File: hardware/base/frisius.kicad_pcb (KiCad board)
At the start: 4 copper layers, 50 x 50 mm, 96 parts, among them J1 MEM2067, J2 USB_C_Receptacle_USB2.0, J3 BATTERY, J4 Display, Q1 Q_Dual_NMOS_G1S2G2D2S1D1, SW1 RESET, SW2 BOOT, SW3 POWER, SW4 NAV, U2 FXOS8700CQR1, U3 MS5637-02BA03, U4 L96-M33, U6 ESP32-S3-WROOM-1, U7 TLV62569DBV, U8 MP2723, U9 MAX17048G

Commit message: schematic complete unreviewed
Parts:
- removed D10, D9: PESD3V3L2UM, Package_TO_SOT_SMD:SOT-883
- removed R59: 0, Resistor_SMD:R_0402_1005Metric
- added C2: 4.7u, Capacitor_SMD:C_0603_1608Metric, F.Cu at (-25.0, 236.4)
- added C26: 1u, Capacitor_SMD:C_0603_1608Metric, F.Cu at (-45.2, 217.1)
- added C27: 1u, Capacitor_SMD:C_0603_1608Metric, F.Cu at (-56.6, 225.8)
- added C28: 0.1u, Capacitor_SMD:C_0402_1005Metric, F.Cu at (-42.8, 223.3)
- added C29: 4.7u, Capacitor_SMD:C_0603_1608Metric, F.Cu at (-41.1, 235.9)
- added C30: 1u, Capacitor_SMD:C_0603_1608Metric, F.Cu at (-40.6, 231.9)
- added C31: 10p, Capacitor_SMD:C_0402_1005Metric, F.Cu at (-37.7, 237.6)
- added C32: 10u, Capacitor_SMD:C_0603_1608Metric, F.Cu at (-50.3, 236.3)
- added C33: 10u, Capacitor_SMD:C_0603_1608Metric, F.Cu at (-45.1, 235.9)
- added C34: 10u, Capacitor_SMD:C_0603_1608Metric, F.Cu at (-24.1, 175.6)
- added C37: 10u, Capacitor_SMD:C_0603_1608Metric, F.Cu at (-23.1, 173.9)
- added C38: 4.7u, Capacitor_SMD:C_0603_1608Metric, F.Cu at (-19.1, 173.9)
- added C39: 0.1u, Capacitor_SMD:C_0402_1005Metric, F.Cu at (-20.6, 175.3)
- added C40: 4.7u, Capacitor_SMD:C_0603_1608Metric, F.Cu at (-11.3, 205.5)
- added C41: 4.7u, Capacitor_SMD:C_0603_1608Metric, F.Cu at (40.8, 115.7)
- added J5: Conn_01x45_Shielded, Connector_FFC-FPC:Hirose_FH12-45S-0.5SH_1x45-1MP_P0.50mm_Horizontal, F.Cu at (99.6, 105.4)
- added J6: CapTouch, Connector_FFC-FPC:TE_0-1734839-8_1x08-1MP_P0.5mm_Horizontal, F.Cu at (115.3, 88.7)
- added J7: I2C ISENSE, Connector_PinHeader_2.54mm:PinHeader_1x04_P2.54mm_Vertical, F.Cu at (66.3, 106.8)
- added L3: 1u, Inductor_SMD:L_Wuerth_MAPI-2510, F.Cu at (-44.9, 232.6)
- added Q2: Q_NMOS_DGS, Package_TO_SOT_SMD:SOT-323_SC-70, F.Cu at (-58.9, 166.6)
- added Q3: Q_NMOS_DGS, Package_TO_SOT_SMD:SOT-323_SC-70, F.Cu at (-54.5, 166.6)
- added R13: 100k, Resistor_SMD:R_0402_1005Metric, F.Cu at (-42.8, 220.3)
- added R14: 100k, Resistor_SMD:R_0402_1005Metric, F.Cu at (-34.1, 216.8)
- added R15: 100k, Resistor_SMD:R_0402_1005Metric, F.Cu at (-37.0, 216.8)
- added R16: 4.7k, Resistor_SMD:R_0402_1005Metric, F.Cu at (-45.7, 221.3)
- added R17: 4.7k, Resistor_SMD:R_0402_1005Metric, F.Cu at (-37.0, 218.8)
- added R18: 4.7k, Resistor_SMD:R_0402_1005Metric, F.Cu at (-37.0, 220.8)
- added R42: R_Shunt, bt_Resistor:R_0805_4WKelvin, F.Cu at (38.0, 116.2)
- added R43: 100k, Resistor_SMD:R_0402_1005Metric, F.Cu at (-34.8, 235.6)
- added R44: 0, Resistor_SMD:R_0402_1005Metric, F.Cu at (-37.7, 235.6)
- added R45: R_Shunt, bt_Resistor:R_0805_4WKelvin, F.Cu at (60.4, 99.0)
- added R46: 0, Resistor_SMD:R_0402_1005Metric, F.Cu at (-37.1, 233.6)
- added R47: 0, Resistor_SMD:R_0402_1005Metric, F.Cu at (-37.1, 231.6)
- added R48: 0, Resistor_SMD:R_0402_1005Metric, F.Cu at (-34.2, 233.6)
- added R49: 0, Resistor_SMD:R_0402_1005Metric, F.Cu at (-34.2, 231.6)
- added R50: R_Shunt, bt_Resistor:R_0805_4WKelvin, F.Cu at (54.9, 121.9)
- added R51: R_Shunt, bt_Resistor:R_0805_4WKelvin, F.Cu at (56.9, 101.3)
- added R52: 0, Resistor_SMD:R_0402_1005Metric, F.Cu at (-6.25, 202.0)
- added R53: 0, Resistor_SMD:R_0402_1005Metric, F.Cu at (-7.89, 205.2)
- added R54: 0, Resistor_SMD:R_0402_1005Metric, F.Cu at (-4.98, 204.0)
- added RN1: 100k, Resistor_SMD:R_Array_Concave_4x0402, F.Cu at (107.9, 109.8)
- added RN2: 100k, Resistor_SMD:R_Array_Concave_4x0402, F.Cu at (103.9, 109.8)
- added RN3: 100k, Resistor_SMD:R_Array_Concave_4x0402, F.Cu at (100.4, 109.8)
- added RN4: 100k, Resistor_SMD:R_Array_Concave_4x0402, F.Cu at (96.9, 109.8)
- added TP12: GPS_RST, TestPoint:TestPoint_Pad_D1.0mm, F.Cu at (-37.8, 166.3)
- added TP13: GPS_INT, TestPoint:TestPoint_Pad_D1.0mm, F.Cu at (-39.2, 170.0)
- added TP14: GPS_FON, TestPoint:TestPoint_Pad_D1.0mm, F.Cu at (-42.2, 170.0)
- added U1: PI4IOE5V9554A, Package_SO:TSSOP-16_4.4x5mm_P0.65mm, F.Cu at (71.7, 89.2)
- added U10: LTR-329ALS-01, Package_LGA:VLGA-4_2x2.5mm_P1.65mm, F.Cu at (-30.0, 177.0)
- added U11: AP2502, Package_TO_SOT_SMD:SOT-23-6, B.Cu at (-16.0, 210.6)
- added U12: PAC1944, Package_DFN_QFN:UQFN-16-1EP_4x4mm_P0.65mm_EP2.7x2.7mm, F.Cu at (61.1, 103.1)
- added U13: TLV62569DBV/AP3428, Package_TO_SOT_SMD:SOT-23-5, F.Cu at (-49.7, 232.8)
- added U14: EClamp2410P, bt_Package_DFN:UDFN-16-4x1.6_P0.5mm_EP3x0.5mm, F.Cu at (44.1, 73.5)
- added U5: FXOS8700CQR1, Package_LGA:LGA-16_3x3mm_P0.5mm_LayoutBorder3x5y, F.Cu at (-24.7, 232.9)
- C11, C9: value 4.7u -> 0.1u; footprint Capacitor_SMD:C_0603_1608Metric -> Capacitor_SMD:C_0402_1005Metric
- C21, C22: value 10u -> 4.7u
- C4: value 4.7u -> 1u
- D1, D3, D5: footprint LED_SMD:LED_0402_1005Metric -> LED_SMD:LED_0603_1608Metric
- D2: footprint LED_SMD:LED_0603_1608Metric -> Diode_SMD:D_SOD-123
- D4: footprint Package_TO_SOT_SMD:SOT-883 -> Package_TO_SOT_SMD:SOT-23
- D6: footprint LED_SMD:LED_0402_1005Metric -> LED_SMD:LED_0603_1608Metric; moved to F.Cu
- D7, D8: value PESD3V3L2UM -> LED_Small_Filled; footprint Package_TO_SOT_SMD:SOT-883 -> LED_SMD:LED_0603_1608Metric
- H1, H2, H3, H4, SW2, SW3, SW4: moved to F.Cu
- J4: value Display -> Debug UART; footprint Connector_Molex:Molex_SlimStack_55560-0241_2x12_P0.50mm_Vertical -> Connector_PinHeader_2.54mm:PinHeader_1x03_P2.54mm_Vertical; moved to F.Cu
- Q1: value Q_Dual_NMOS_G1S2G2D2S1D1 -> Q_NMOS_DGS; footprint Package_TO_SOT_SMD:SOT-363_SC-70-6 -> Package_TO_SOT_SMD:SOT-323_SC-70
- R1, R6: value R_Small -> 100k
- R10, R11, R12, R8: value 10k -> 100k
- R2, R7: value 10k -> 1k
- R34: value 0 -> 14k
- R35: value 14k -> ?
- R40: value R_Small -> 4.7k
- U2: value FXOS8700CQR1 -> 74CBTLV3257; footprint Package_LGA:LGA-16_3x3mm_P0.5mm_LayoutBorder3x5y -> Package_SO:TSSOP-16_4.4x5mm_P0.65mm
- U3: value MS5637-02BA03 -> ESP32-S3-WROOM-1-PinOrder; footprint bt_Package_LGA:TE_MS563702BA03-50 -> bt_Espressif:ESP32-S3-WROOM-1U
- U6: value ESP32-S3-WROOM-1 -> MS5637-02BA03; footprint bt_Espressif:ESP32-S3-WROOM-1U -> bt_Package_LGA:TE_MS563702BA03-50
- U7: value TLV62569DBV -> TLV62569DBV/AP3428
- moved R40 171.1 mm to (-53.2, 225.5), turned to 0 degrees
- moved SW2 158.6 mm to (-38.6, 226.6), turned to 0 degrees
- moved R10 157.7 mm to (-45.7, 219.3), turned to 0 degrees
- moved C14 157.0 mm to (-21.0, 233.6), turned to 0 degrees
- moved R8 156.7 mm to (-31.4, 228.9), turned to 0 degrees
- moved C13 156.3 mm to (-18.7, 235.5)
- moved C15 152.1 mm to (-21.6, 236.1), turned to 0 degrees
- moved C16 152.1 mm to (-15.2, 231.6)
- moved C12 151.7 mm to (-18.1, 233.6), turned to 0 degrees
- moved R12 151.6 mm to (-39.9, 220.3), turned to 0 degrees
- moved R9 150.5 mm to (-21.0, 231.6), turned to 0 degrees
- moved C11 149.8 mm to (-18.1, 231.6), turned to 0 degrees
- moved R11 147.3 mm to (-34.1, 218.8), turned to 0 degrees
- moved C3 143.2 mm to (-26.5, 219.8)
- moved SW1 142.1 mm to (-26.1, 202.5)
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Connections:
- C1 pad 1: +3V3 -> VDD_CORE_3V3
- C11 pad 1: +3V3 -> VDD_AUX_3V3
- C12 pad 1: +3V3 -> VDD_AUX_3V3
- C13 pad 1: +3V3 -> Net-(C13-Pad1)
- C14 pad 1: Net-(C14-Pad1) -> VDD_AUX_3V3
- C15 pad 1: +3V3 -> VDD_AUX_3V3
- C17 pad 1: VDD_NVDC -> VDD_AUX_3V3
- C18 pad 1: +3V3 -> VDD_AUX_3V3
- C19 pad 1: +3V3 -> VDD_AUX_3V3
- C21 pad 1: /Power/VREF -> VBUS
- C22 pad 1: +BATT -> VBUS
- C3 pad 1: +3V3 -> VDD_AUX_3V3
- C35 pad 1: VBUS -> Net-(C35-Pad1)
- C36 pad 1: VBUS -> Net-(C35-Pad1)
- C6 pad 1: +3V3 -> Net-(C6-Pad1)
- C7 pad 1: +3V3 -> VDD_CORE_3V3
- C8 pad 1: +3V3 -> VDD_CORE_3V3
- C9 pad 1: VBUS -> VDD_AUX_3V3
- D2 pad 1: Net-(D2-Pad1) -> /Power/CORE_ENABLE
- D2 pad 2: Net-(D2-Pad2) -> /Power/BOOTSTRAP
- D5 pad 1: GND -> Net-(D5-Pad1)
- D7 pad 1: /Processor/SDMMC.D0 -> GND
- D7 pad 2: /Processor/SDMMC.D1 -> Net-(D7-Pad2)
- D8 pad 1: /Processor/SDMMC.CMD -> GND
- D8 pad 2: /Processor/SDMMC.CLK -> Net-(D8-Pad2)
- J1 pad 1: /Processor/SDMMC.D2 -> Net-(J1-Pad1)
- J1 pad 2: /Processor/SDMMC.D3 -> Net-(J1-Pad2)
- J1 pad 3: /Processor/SDMMC.CMD -> Net-(J1-Pad3)
- J1 pad 4: +3V3 -> VDD_AUX_3V3
- J1 pad 5: /Processor/SDMMC.CLK -> Net-(J1-Pad5)
- J1 pad 7: /Processor/SDMMC.D0 -> Net-(J1-Pad7)
- J1 pad 8: /Processor/SDMMC.D1 -> Net-(J1-Pad8)
- J2 pad A4: VBUS -> Net-(C35-Pad1)
- J2 pad A9: VBUS -> Net-(C35-Pad1)
- J2 pad B4: VBUS -> Net-(C35-Pad1)
- J2 pad B9: VBUS -> Net-(C35-Pad1)
- J4 pad 2: GND -> /Processor/DEBUG_RX
- J4 pad 3: +3V3 -> /Processor/DEBUG_TX
- L1 pad 2: +3V3 -> Net-(C6-Pad1)
- Q1 pad 1: Net-(D2-Pad2) -> Net-(D5-Pad1)
- Q1 pad 2: GND -> /GPS/GPS_FIX
- Q1 pad 3: /Power/SHUTDOWN -> GND
- R1 pad 1: +3V3 -> VDD_CORE_3V3
- R1 pad 2: /Processor/RST_BTN -> ~{RESET}
- R10 pad 1: +3V3 -> VDD_AUX_3V3
- R10 pad 2: /Processor/SDMMC.CMD -> /Display/IM2
- R11 pad 1: +3V3 -> /Display/IM2
- R11 pad 2: /Processor/SDMMC.D3 -> GND
- R12 pad 1: +3V3 -> VDD_AUX_3V3
- R12 pad 2: /Processor/SDMMC.D2 -> /Display/IM1
- R2 pad 1: Net-(R2-Pad1) -> Net-(D7-Pad2)
- R2 pad 2: GND -> /Processor/STATUS_IOEXP0
- R23 pad 2: +3V3 -> VDD_CORE_3V3
- R24 pad 1: /Power/PORT_D- -> /Power/PORT_D+
- R24 pad 2: /Power/USB_CHG.D- -> /Power/USB_CHG.D+
- R25 pad 1: /Power/PORT_D+ -> /Power/PORT_D-
- R25 pad 2: /Power/USB_CHG.D+ -> /Power/USB_CHG.D-
- R27 pad 1: Net-(D2-Pad1) -> /Power/CORE_ENABLE
- R27 pad 2: +3V3 -> VDD_CORE_3V3
- R28 pad 2: /GPS/L96_FIX -> VDD_AUX_3V3
- R29 pad 1: +3V3 -> Net-(C6-Pad1)
- R3 pad 1: +3V3 -> VDD_AUX_3V3
- R31 pad 1: /Power/VREF -> Net-(C37-Pad1)
- R32 pad 1: /Power/VREF -> Net-(C37-Pad1)
- R33 pad 1: Net-(R33-Pad1) -> /Power/PORT_D+
- R33 pad 2: GND -> /Power/USB_ESP.D+
- R35 pad 1: Net-(R35-Pad1) -> Net-(C31-Pad1)
- R35 pad 2: GND -> Net-(C31-Pad2)
- R37 pad 2: Net-(R36-Pad2) -> Net-(R36-Pad1)
- R4 pad 1: +3V3 -> VDD_AUX_3V3
- R40 pad 1: +3V3 -> /Display/SYS_I2C.SCL
- R40 pad 2: /Processor/NAV_BTN -> VDD_AUX_3V3
- R41 pad 2: Net-(R41-Pad2) -> /Processor/STATUS_ESP
- R6 pad 1: +3V3 -> VDD_CORE_3V3
- R7 pad 1: +3V3 -> Net-(D8-Pad2)
- R7 pad 2: /Processor/SDMMC.D1 -> /Processor/STATUS_IOEXP1
- R8 pad 1: +3V3 -> VDD_CORE_3V3
- R8 pad 2: /Processor/SDMMC.D0 -> /Processor/NAV_BTN
- R9 pad 1: +3V3 -> Net-(R9-Pad1)
- R9 pad 2: /Processor/SDMMC.CLK -> GND
- SW1 pad 2: /Processor/RST_BTN -> ~{RESET}
- SW3 pad 2: Net-(D2-Pad2) -> /Power/BOOTSTRAP
- U2 pad 1: +3V3 -> /Display/LCD_SPI_CS
- U2 pad 10: GND -> /Display/LCD_CTRL.HSYNC
- U2 pad 11: unconnected-(U2-Pad11) -> /Display/LCD_SPI.MOSI
- U2 pad 12: GND -> /Display/LCD_MUX3
- U2 pad 13: GND -> /Display/LCD_CTRL.VSYNC
- U2 pad 14: +3V3 -> /Display/LCD_SPI.MISO
- U2 pad 15: unconnected-(U2-Pad15) -> GND
- U2 pad 16: Net-(R2-Pad1) -> VDD_AUX_3V3
- U2 pad 2: Net-(C14-Pad1) -> /Display/LCD_SPI.DC
- U2 pad 3: GND -> /Display/LCD_CTRL.DE
- U2 pad 4: /Display/SYS_I2C.SCL -> /Display/LCD_MUX0
- U2 pad 5: GND -> /Display/LCD_SPI.SCLK
- U2 pad 6: /Display/SYS_I2C.SDA -> /Display/LCD_CTRL.PCLK
- U2 pad 7: GND -> /Display/LCD_MUX1
- U2 pad 8: Net-(C16-Pad1) -> GND
- U2 pad 9: unconnected-(U2-Pad9) -> /Display/LCD_MUX2
- U3 pad 1: +3V3 -> GND
- U3 pad 2: /Display/SYS_I2C.SDA -> VDD_CORE_3V3
- U3 pad 3: /Display/SYS_I2C.SCL -> ~{RESET}
- U3 pad 4: GND -> /Processor/SDMMC.D3
- U4 pad 2: /GPS/L96_FIX -> /GPS/GPS_FIX
- U4 pad 23: Net-(TP12-Pad1) -> ~{RESET}
- U4 pad 28: Net-(TP14-Pad1) -> /GPS/GPS_FORCE_ON
- U4 pad 8: VDD_NVDC -> VDD_AUX_3V3
- U4 pad 9: +3V3 -> VDD_AUX_3V3
- U6 pad 1: GND -> VDD_AUX_3V3
- U6 pad 2: +3V3 -> /Display/SYS_I2C.SDA
- U6 pad 3: /Processor/RST_BTN -> /Display/SYS_I2C.SCL
- U6 pad 4: unconnected-(U6-Pad4) -> GND
- U7 pad 1: Net-(D2-Pad1) -> /Power/CORE_ENABLE
- U8 pad 11: Net-(R36-Pad2) -> Net-(R36-Pad1)
- U8 pad 12: Net-(R36-Pad1) -> Net-(R36-Pad2)
- U8 pad 13-14: /Power/VREF -> Net-(C37-Pad1)
- U8 pad 17: +BATT -> Net-(R50-Pad1)
- U8 pad 18: Net-(R34-Pad1) -> Net-(R46-Pad1)
- U8 pad 23: Net-(R33-Pad1) -> Net-(R44-Pad1)
- U8 pad 24: Net-(R35-Pad1) -> Net-(R34-Pad1)
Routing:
- net /Display/SYS_I2C.SDA: track 24.3 -> 0.00 mm, vias 4 -> 0
- added copper zone on F.Cu, net VDD_AUX_3V3
- removed copper zone on F.Cu, net +3V3
- removed copper zone on In2.Cu, net +3V3
- removed copper zone on B.Cu, net GND
- removed copper zone on F.Cu, net GND
- removed copper zone on In1.Cu, net GND
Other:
- board size 50 x 50 mm -> 100 x 85 mm
- board text added: "3V GND RST TI TD TC SO SI SC DC CS"
- board text added: "BL R0 R1 G0 G1 B0 B1 DE PC HS VS"

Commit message: placed components on board - rough
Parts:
- removed C40: 4.7u, Capacitor_SMD:C_0603_1608Metric
- TP12, TP13, TP14: moved to B.Cu
- U11: moved to F.Cu
- moved SW2 220.1 mm to (108.6, 63.0), turned to 180 degrees
- moved R40 218.7 mm to (114.7, 85.3), turned to 90 degrees
- moved R16 212.5 mm to (117.7, 85.3), turned to 90 degrees
- moved C28 207.2 mm to (113.3, 87.1), turned to 180 degrees
- moved R18 204.0 mm to (115.7, 85.3), turned to 90 degrees
- moved SW3 203.6 mm to (98.6, 63.0), turned to 180 degrees
- moved R17 203.5 mm to (116.7, 85.3), turned to 90 degrees
- moved R8 203.0 mm to (88.6, 65.2)
- moved SW4 202.9 mm to (88.6, 63.0)
- moved R6 198.5 mm to (108.6, 65.2), turned to 180 degrees
- moved R13 189.3 mm to (111.9, 111.3), turned to 90 degrees
- moved R10 189.1 mm to (110.9, 113.3), turned to 90 degrees
- moved R12 185.7 mm to (111.9, 113.3), turned to 90 degrees
- moved C27 185.7 mm to (89.3, 110.9), turned to 180 degrees
- moved R15 183.3 mm to (112.9, 111.3), turned to 90 degrees
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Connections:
- C17 pad 1: VDD_AUX_3V3 -> VDD_NVDC
- U12 pad 10: /Power/VAUX_S+ -> /Power/VCORE_S+
- U12 pad 7: /Power/VCORE_S- -> /Power/VAUX_S-
- U12 pad 8: /Power/VCORE_S+ -> /Power/VAUX_S+
- U12 pad 9: /Power/VAUX_S- -> /Power/VCORE_S-
- U3 pad 15: /Display/LCD_RGB.R2 -> /Display/LCD_RGB.R0
- U3 pad 17: /Display/LCD_RGB.R0 -> /Display/LCD_RGB.R2
- U3 pad 18: /Display/LCD_RGB.G2 -> /Display/LCD_RGB.G0
- U3 pad 20: /Display/LCD_RGB.G0 -> /Display/LCD_RGB.G2
- U3 pad 21: /Display/LCD_RGB.B1 -> /Display/LCD_RGB.B0
- U3 pad 22: /Display/LCD_RGB.B0 -> /Display/LCD_RGB.B1
- U4 pad 8: VDD_AUX_3V3 -> VDD_NVDC
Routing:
- net VDD_NVDC: track 0.00 -> 11.9 mm
- net Net-(C10-Pad2): track 0.00 -> 9.25 mm
- net Net-(R50-Pad1): track 0.00 -> 5.85 mm
- net VBUS: track 0.00 -> 4.59 mm
- net Net-(C23-Pad1): track 0.00 -> 2.47 mm
- net Net-(C37-Pad1): track 0.00 -> 2.35 mm
- net Net-(R46-Pad1): track 0.00 -> 1.94 mm
- net Net-(C10-Pad1): track 0.00 -> 1.16 mm
- added copper zone on F.Cu, net GND
- removed copper zone on F.Cu, net Net-(C10-Pad2)
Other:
- outline, holes or cut-outs redrawn

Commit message: further placement, pre condense
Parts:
- moved U1 19.2 mm to (78.4, 78.4), turned to 180 degrees
- moved R23 16.1 mm to (32.7, 85.0), turned to 0 degrees
- moved Q2 14.6 mm to (32.7, 86.9), turned to 0 degrees
- moved R45 13.5 mm to (51.7, 85.5), turned to 0 degrees
- moved R51 13.5 mm to (63.4, 85.3), turned to 0 degrees
- moved L1 10.8 mm to (46.3, 85.4), turned to 0 degrees
- moved L3 10.8 mm to (57.8, 85.3), turned to 0 degrees
- moved D2 10.7 mm to (34.5, 89.5), turned to 180 degrees
- moved Q3 10.7 mm to (36.2, 86.9), turned to 180 degrees
- moved C8 8.89 mm to (50.3, 88.4), turned to -90 degrees
- moved C33 8.65 mm to (61.9, 88.4), turned to -90 degrees
- moved R25 8.54 mm to (43.4, 118.0)
- moved R34 8.54 mm to (44.5, 118.0)
- moved R24 8.54 mm to (42.3, 118.0)
- moved R44 8.54 mm to (45.6, 118.0)
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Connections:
- J7 pad 2: /Power/ISENSE_SCL -> /Power/ISENSE_SDA
- J7 pad 3: /Power/ISENSE_SDA -> /Power/ISENSE_SCL
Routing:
- net /Power/VBUS_S+: track 0.00 -> 19.4 mm
- net /Power/VBUS_S-: track 0.00 -> 18.9 mm
- net /Power/VBAT_S-: track 0.00 -> 17.3 mm
- net /Power/VBAT_S+: track 0.00 -> 16.9 mm
- net /Processor/SDMMC.D3: track 0.00 -> 12.1 mm
- net /Power/VCORE_S+: track 0.00 -> 11.8 mm
- net /Processor/SDMMC.D2: track 0.00 -> 11.7 mm
- net /Processor/SDMMC.CLK: track 0.00 -> 11.6 mm
- net /Processor/SDMMC.CMD: track 0.00 -> 11.5 mm
- net /Power/VCORE_S-: track 0.00 -> 11.4 mm
- net /Processor/SDMMC.D0: track 0.00 -> 11.2 mm
- net /Processor/SDMMC.D1: track 0.00 -> 10.9 mm
- net /Power/VAUX_S+: track 0.00 -> 9.00 mm
- net /Power/VAUX_S-: track 0.00 -> 9.00 mm
- net Net-(C35-Pad1): track 0.00 -> 8.61 mm
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
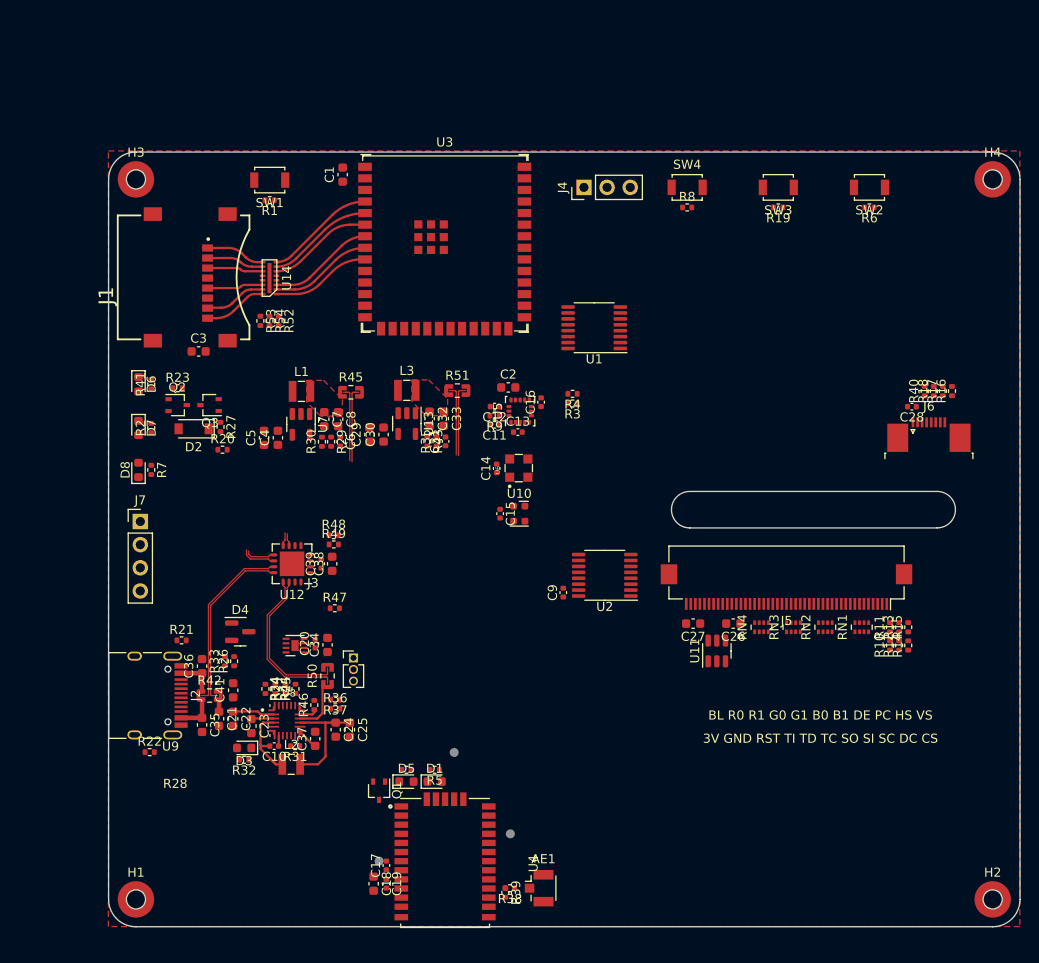
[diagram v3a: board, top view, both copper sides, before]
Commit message: Testing condensed layout
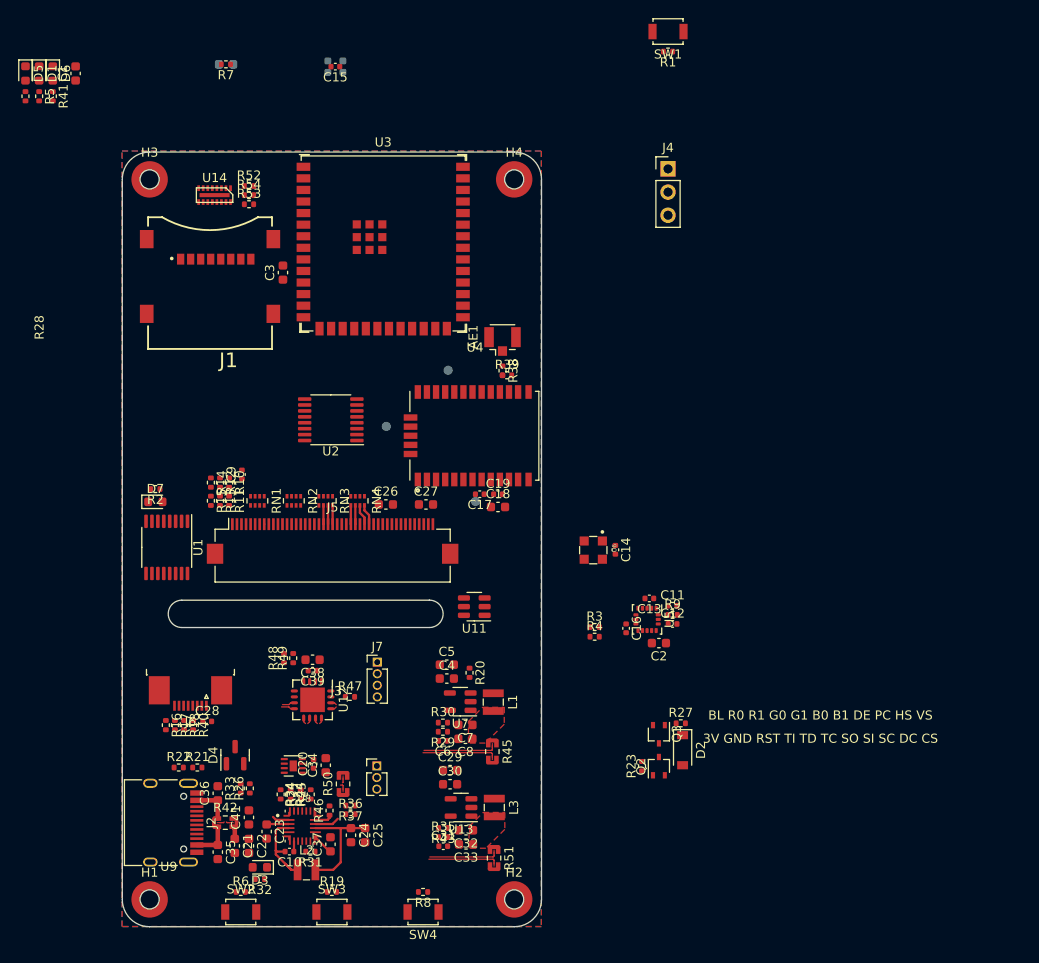
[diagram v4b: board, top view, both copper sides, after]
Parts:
- removed Q1: Q_NMOS_DGS, Package_TO_SOT_SMD:SOT-323_SC-70
- D8, U10: moved to B.Cu
- J7: footprint Connector_PinHeader_2.54mm:PinHeader_1x04_P2.54mm_Vertical -> Connector_PinHeader_1.27mm:PinHeader_1x04_P1.27mm_Vertical
- moved SW2 105.3 mm to (39.6, 142.5), turned to 0 degrees
- moved R6 102.0 mm to (39.6, 140.3), turned to 0 degrees
- moved R16 93.7 mm to (31.4, 122.0), turned to -90 degrees
- moved SW3 93.4 mm to (49.6, 142.5), turned to 0 degrees
- moved R17 91.9 mm to (32.4, 122.0), turned to -90 degrees
- moved R18 90.1 mm to (33.4, 122.0), turned to -90 degrees
- moved R19 89.7 mm to (49.6, 140.3), turned to 0 degrees
- moved D1 89.0 mm to (17.5, 50.5), turned to -90 degrees
- moved D5 88.2 mm to (16.0, 50.5), turned to -90 degrees
- moved R40 88.2 mm to (34.4, 122.0), turned to -90 degrees
- moved J6 85.9 mm to (34.1, 118.5), turned to 180 degrees
- moved R5 85.7 mm to (17.5, 53.0), turned to -90 degrees
- moved R28 84.9 mm to (16.0, 53.0), turned to -90 degrees
- moved C28 84.7 mm to (35.9, 121.6), turned to 0 degrees
- moved SW4 84.6 mm to (59.6, 142.5), turned to 180 degrees
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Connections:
- D5 pad 1: Net-(D5-Pad1) -> GND
- J5 pad 37: /Display/LCDK4 -> /Display/LCDK1
- J5 pad 38: /Display/LCDK3 -> /Display/LCDK2
- J5 pad 39: /Display/LCDK2 -> /Display/LCDK3
- J5 pad 40: /Display/LCDK1 -> /Display/LCDK4
- J7 pad 2: /Power/ISENSE_SDA -> /Power/ISENSE_SCL
- J7 pad 3: /Power/ISENSE_SCL -> /Power/ISENSE_SDA
- R28 pad 2: VDD_AUX_3V3 -> /GPS/GPS_FIX
- U3 pad 23: /Display/SYS_I2C.SCL -> /Display/LCD_MUX0
- U3 pad 24: /Display/SYS_I2C.SDA -> /Display/LCD_MUX1
- U3 pad 25: /Processor/IOEXP_INT -> /Display/LCD_MUX2
- U3 pad 26: /Display/TOUCH_INT -> /Display/LCD_MUX3
- U3 pad 32: /Display/LCD_MUX0 -> /Display/SYS_I2C.SCL
- U3 pad 33: /Display/LCD_MUX1 -> /Display/SYS_I2C.SDA
- U3 pad 34: /Display/LCD_MUX2 -> /Processor/IOEXP_INT
- U3 pad 35: /Display/LCD_MUX3 -> /Display/TOUCH_INT
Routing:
- net /Power/VBUS_S+: track 19.4 -> 1.24 mm
- net /Power/VBUS_S-: track 18.9 -> 1.24 mm
- net /Power/VBAT_S-: track 17.3 -> 1.46 mm
- net /Power/VBAT_S+: track 16.9 -> 1.24 mm
- net /Processor/SDMMC.D3: track 12.1 -> 0.00 mm
- net /Processor/SDMMC.D2: track 11.7 -> 0.00 mm
- net /Processor/SDMMC.CLK: track 11.6 -> 0.00 mm
- net /Processor/SDMMC.CMD: track 11.5 -> 0.00 mm
- net /Processor/SDMMC.D0: track 11.2 -> 0.00 mm
- net /Processor/SDMMC.D1: track 10.9 -> 0.00 mm
- net Net-(J1-Pad8): track 6.95 -> 0.00 mm
- net Net-(J1-Pad7): track 6.73 -> 0.00 mm
- net Net-(J1-Pad1): track 6.50 -> 0.00 mm
- net Net-(J1-Pad2): track 6.28 -> 0.00 mm
- net Net-(J1-Pad3): track 6.13 -> 0.00 mm
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- added copper zone on B.Cu, net GND
- added copper zone on In1.Cu, net GND
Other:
- board size 100 x 85 mm -> 46 x 85 mm
